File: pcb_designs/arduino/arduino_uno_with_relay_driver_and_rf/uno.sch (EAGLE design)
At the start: 53 parts, among them IC1 ATMEGA328, IC2 7805, Q1 12MHZ, T1 BC547, T2 BC547, T3 BC547, T4 BC547

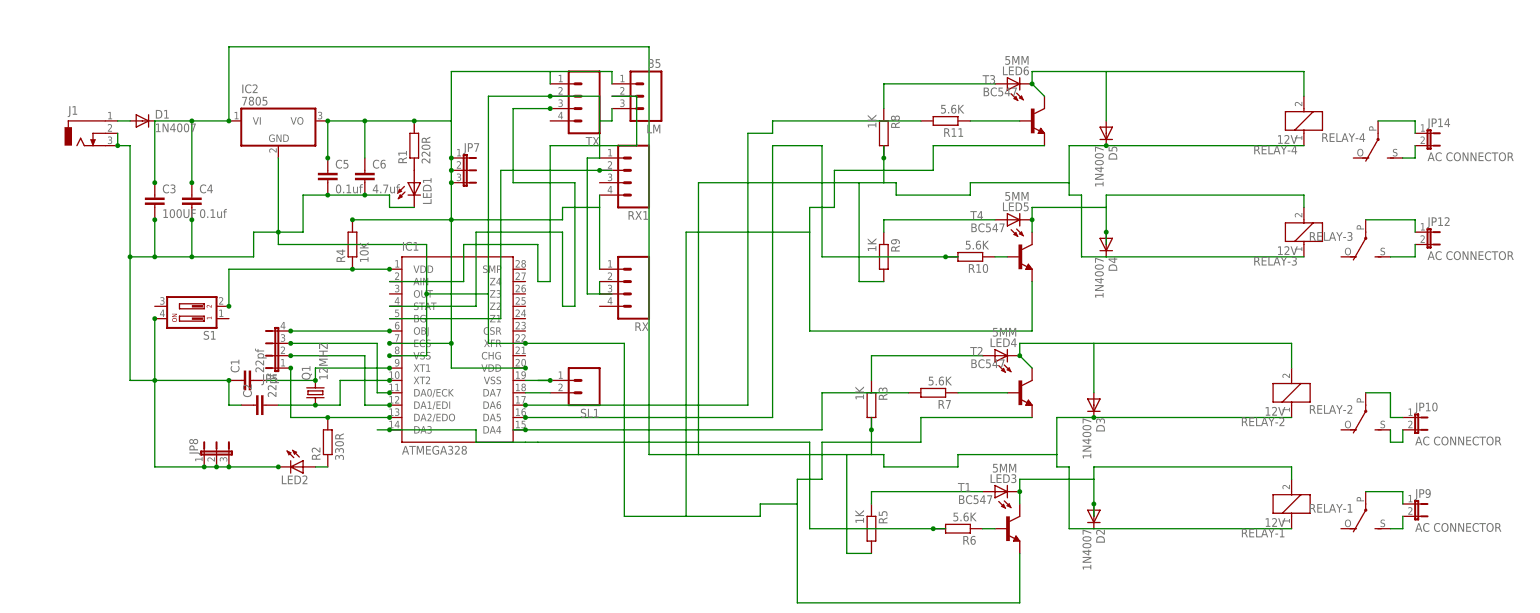
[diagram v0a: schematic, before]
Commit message: 
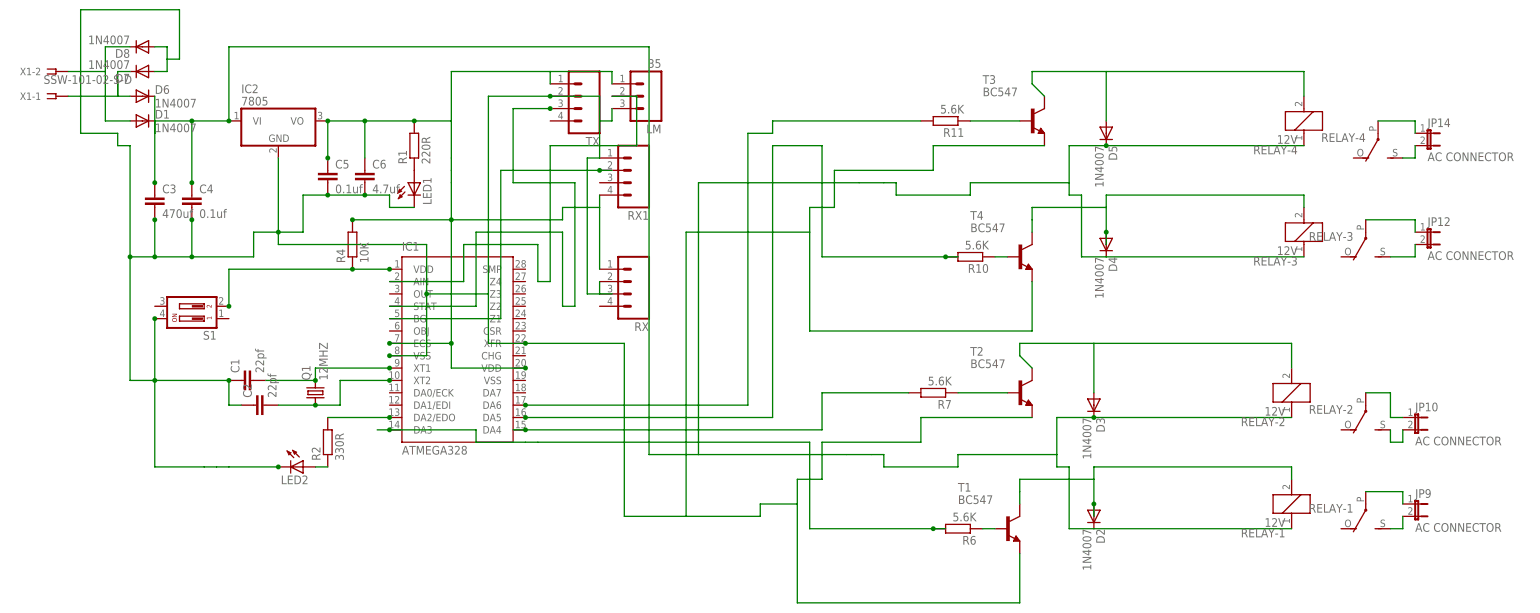
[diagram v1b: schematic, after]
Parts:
- removed J1: (no value), con-jack:DCJ0303
- removed JP5: (no value), jumper:JP4E
- removed JP7, JP8: (no value), jumper:JP2E
- removed LED3, LED4, LED5, LED6: 5MM, led:LED5MM
- removed R3, R5, R8, R9: 1K, rcl:R-EU_0204/7
- removed SL1: (no value), con-amp-quick:M02
- added D6, D7, D8: 1N4007, diode:1N4004
- added X1: SSW-101-02-S-D, con-samtec:SSW-101-02-S-D
- C3: value 100UF -> 470uf
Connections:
- removed net N$18: IC1.OBJ, JP5.4
- removed net N$19: IC1.DA1/EDI, JP5.2
- removed net N$20: IC1.DA0/ECK, JP5.3
- removed net N$27: IC1.VSS@1, SL1.1
- removed net N$3: D1.A, J1.1
- removed net N$33: LED3.A, R5.1
- removed net N$34: LED4.A, R3.1
- removed net N$47: LED5.A, R9.1
- removed net N$48: LED6.A, R8.1
- removed net N$5: IC1.DA7, SL1.2
- new net N$10: D6.A, D7.C, X1-1.1
- new net N$12: D1.A, D8.C, X1-2.1
- net N$21: no longer JP5.1
- net N$28: no longer LED3.C
- net N$4: no longer JP7.1, JP7.2, JP7.3
- net N$42: no longer LED4.C
- net N$43: no longer LED5.C
- net N$55: now also D7.A, D8.A; no longer J1.2, J1.3, JP8.1, JP8.2, JP8.3
- net N$58: no longer LED6.C
- net N$7: now also D6.C; no longer R3.2, R5.2, R8.2, R9.2
